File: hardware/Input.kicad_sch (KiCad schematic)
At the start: 40 parts, among them J1 USB_C_Receptacle_USB2.0, J2 Barrel_Jack_Switch, J4 AudioJack3, J5 Conn_Coaxial, J6 Conn_Coaxial, J7 Conn_Coaxial, J8 Conn_Coaxial, U23 74LVCH2T45DC, U24 74LVCH2T45DC, U25 74LVCH2T45DC

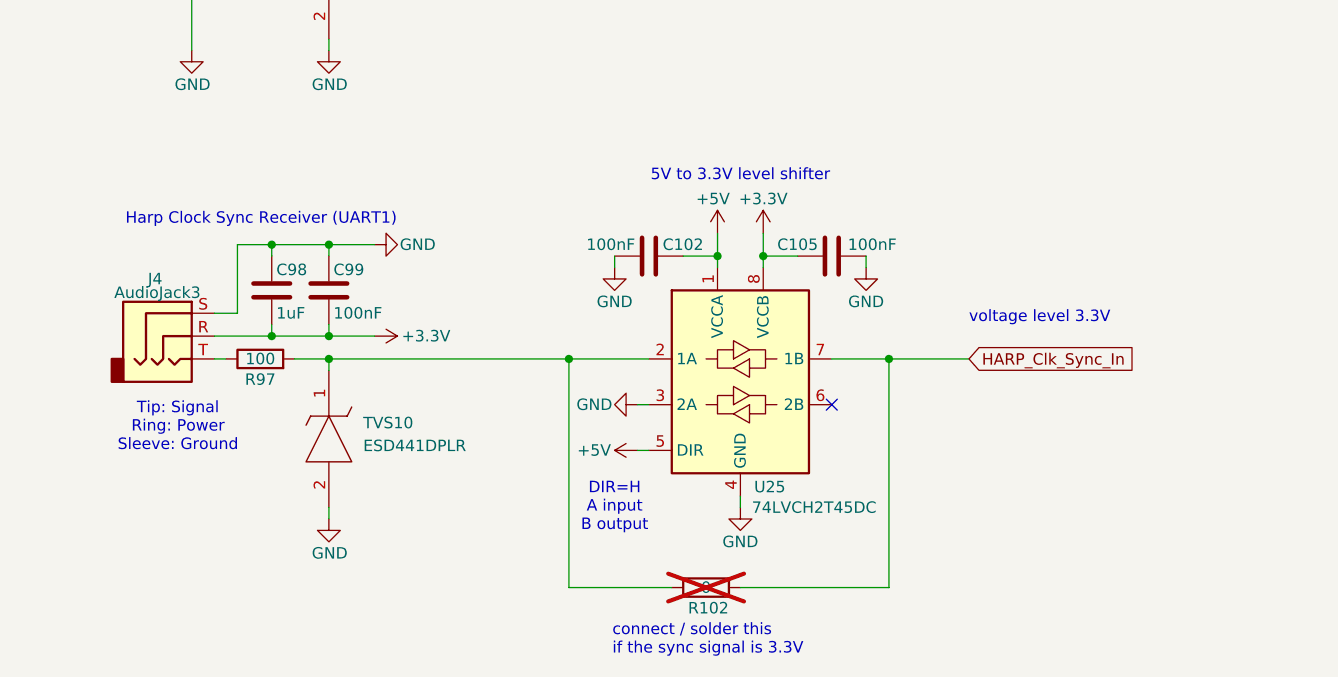
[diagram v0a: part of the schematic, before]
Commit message: draft simplified rp2350 schematic w/sd card
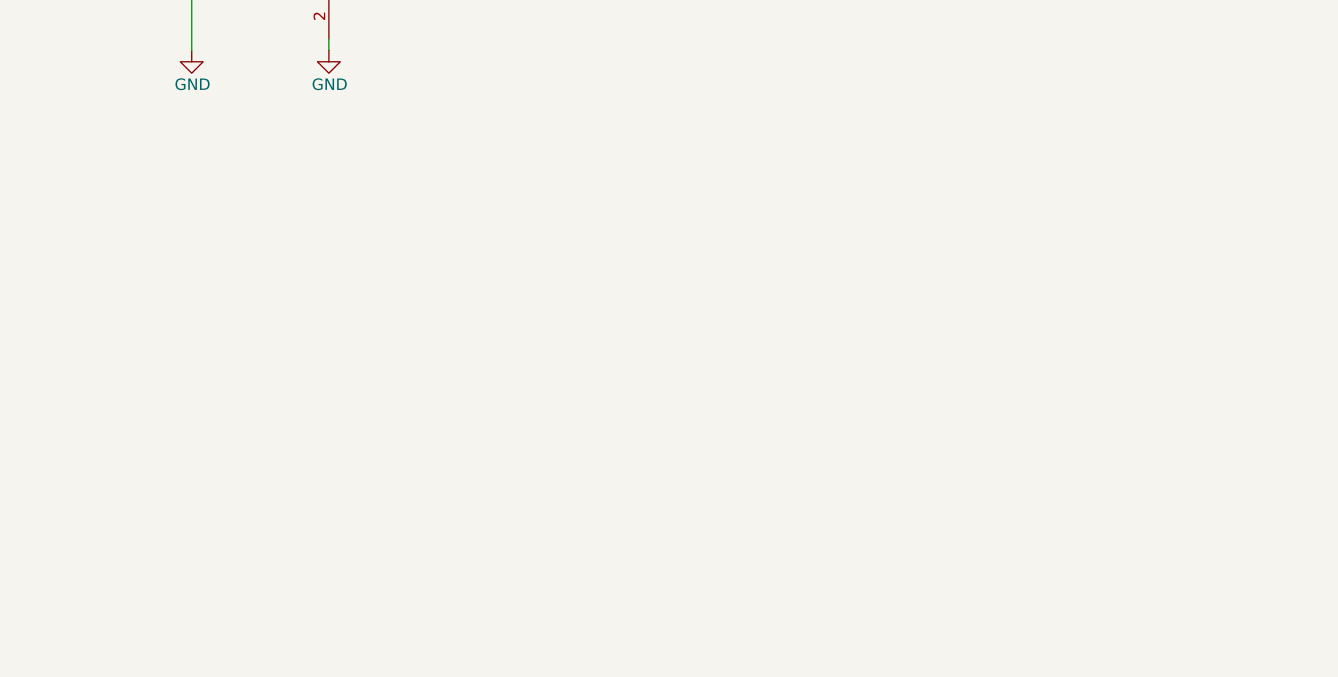
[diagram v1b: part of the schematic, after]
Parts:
- removed C102, C105, C99: 100nF, Capacitor_SMD:C_0603_1608Metric, symbol harp.device.quad.dac:C_0603
- removed C98: 1uF, Capacitor_SMD:C_0603_1608Metric, symbol harp.device.quad.dac:C_0603
- removed J4: AudioJack3, harp.device.quad.dac.kicad:Jack_3.5mm_CUI_SJ-3524-SMT_Horizontal, symbol harp.device.quad.dac:AudioJack3
- removed R102: 0, Resistor_SMD:R_0603_1608Metric, symbol harp.device.quad.dac:R_0603
- removed R97: 100, Resistor_SMD:R_0603_1608Metric, symbol harp.device.quad.dac:R_0603
- removed TVS10: ESD441DPLR, harp.device.quad.dac.kicad:ESD441DPLR, symbol harp.device.quad.dac:ESD441DPLR
- removed U25: 74LVCH2T45DC, harp.device.quad.dac.kicad:VSSOP-8_2.3x2mm_P0.5mm, symbol harp.device.quad.dac:74LVCH2T45DC
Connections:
- no-connect marks 8 -> 7
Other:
- note removed: "Harp Clock Sync Receiver (UART1)"
- note removed: "Tip: Signal Ring: Power Sleeve: Ground"
- note removed: "connect / solder this if the sync signal is 3.3V"

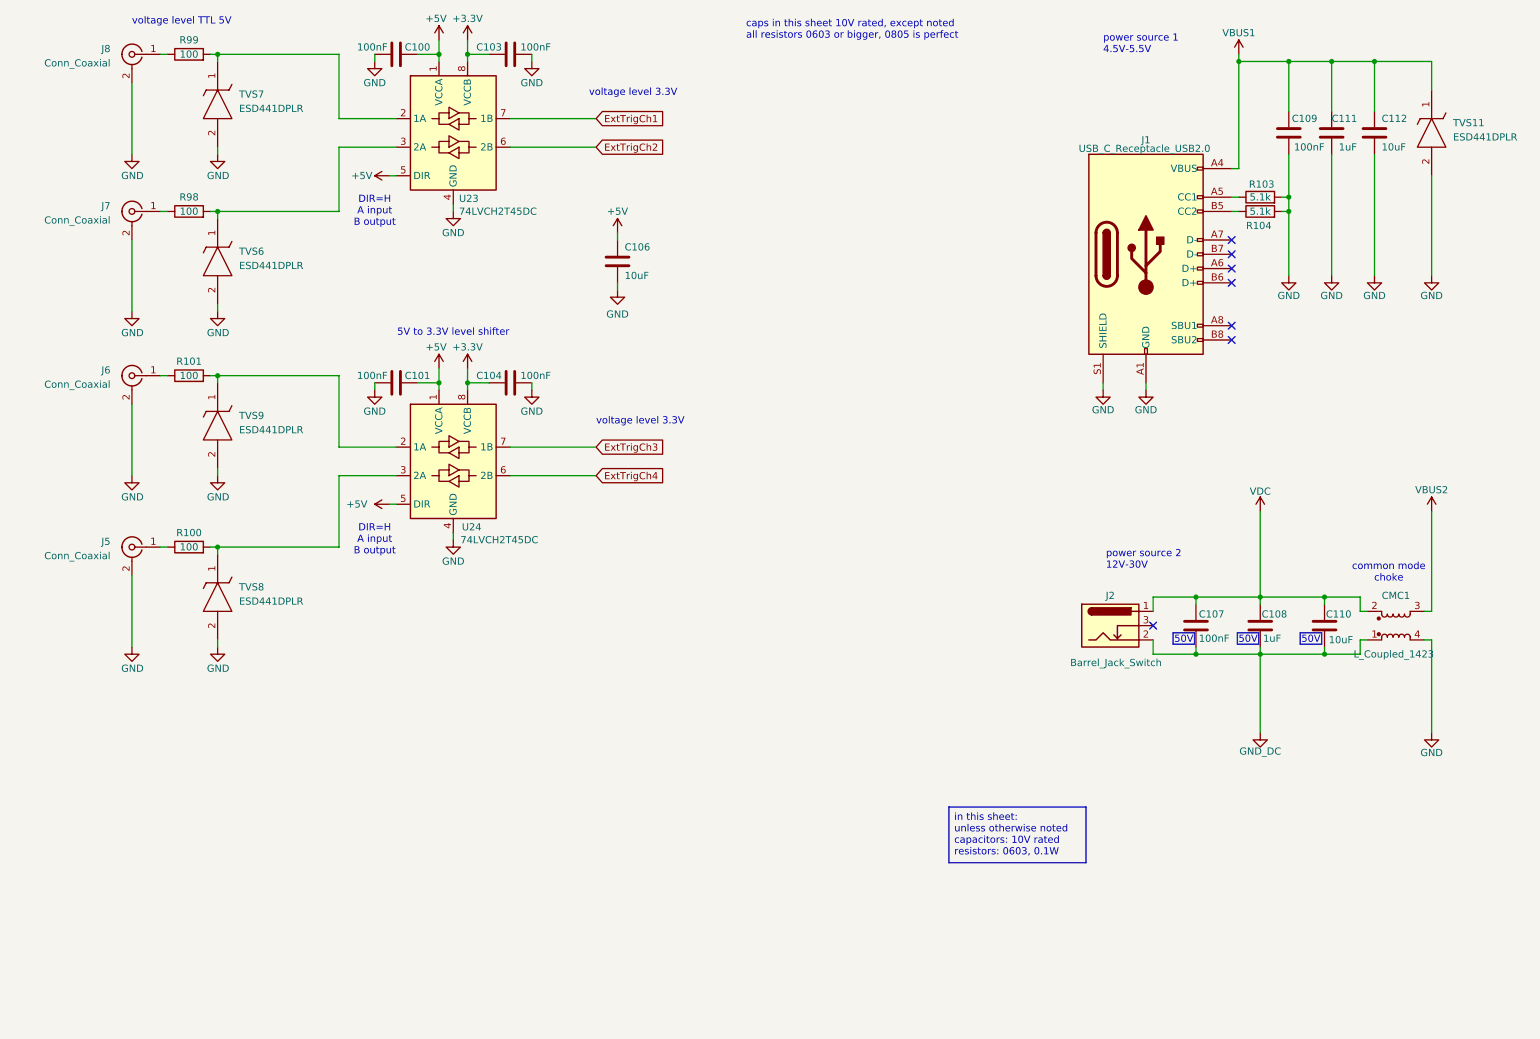
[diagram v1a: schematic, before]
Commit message: draft new analog signal chain & short-circuit detection
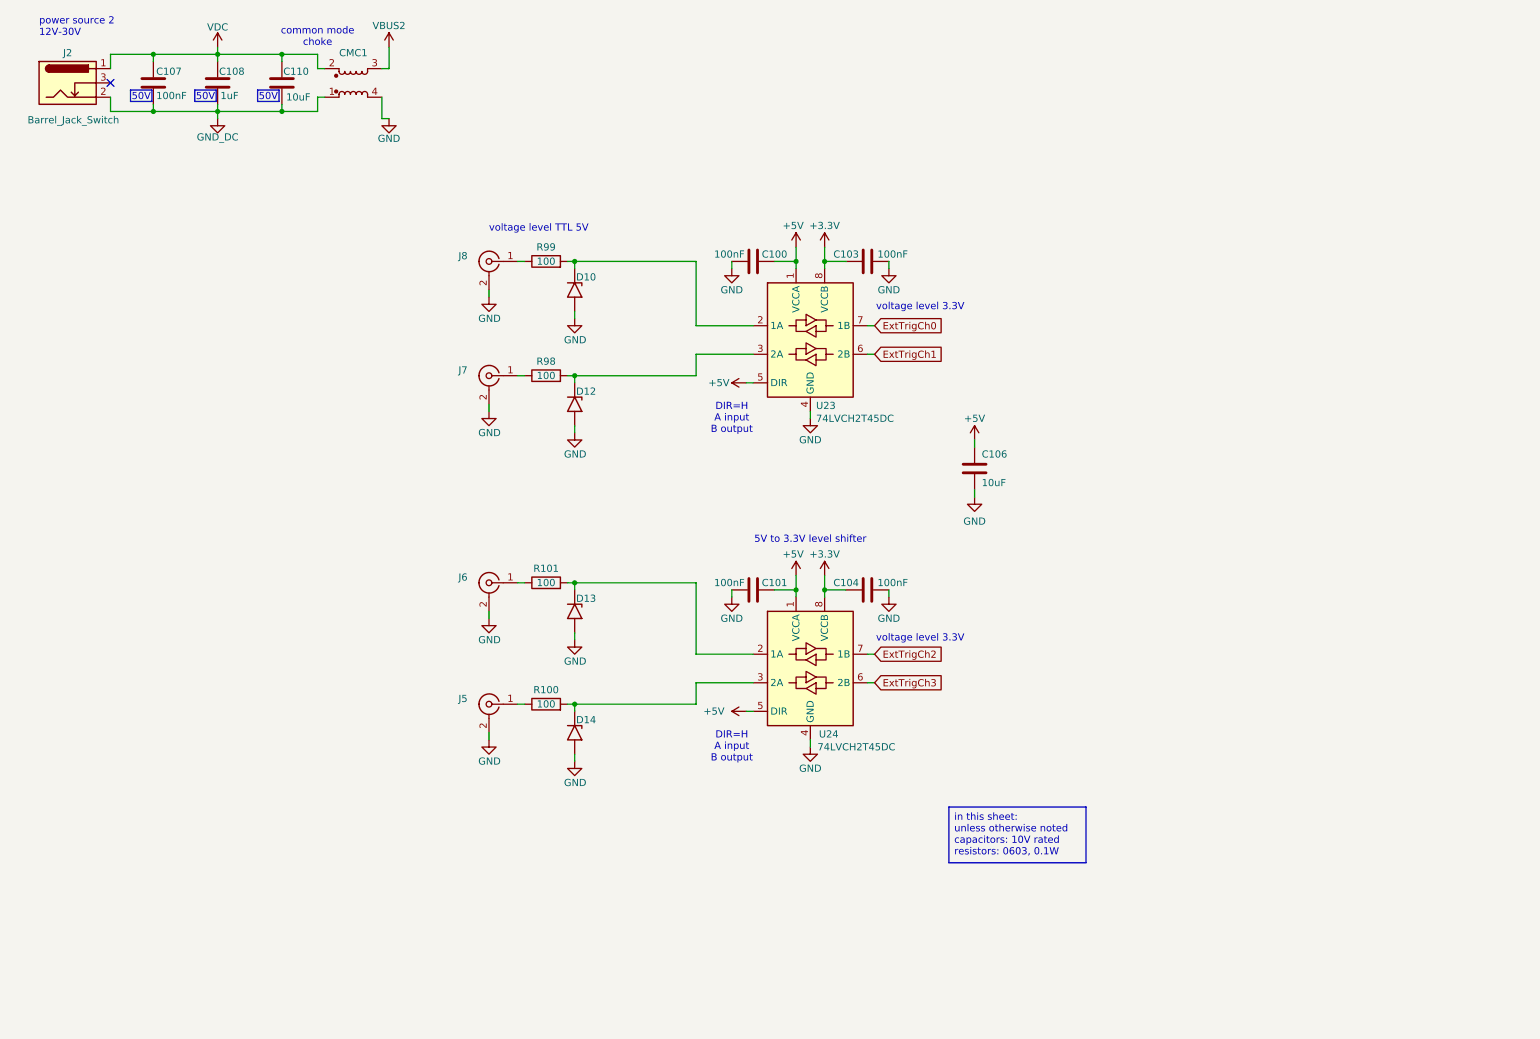
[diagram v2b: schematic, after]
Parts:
- removed C109: 100nF, Capacitor_SMD:C_0603_1608Metric, symbol harp.device.quad.dac:C_0603
- removed C111: 1uF, Capacitor_SMD:C_0603_1608Metric, symbol harp.device.quad.dac:C_0603
- removed C112: 10uF, Capacitor_SMD:C_0603_1608Metric, symbol harp.device.quad.dac:C_0603
- removed J1: USB_C_Receptacle_USB2.0, harp.device.quad.dac.kicad:USB_C_Receptacle_JAE_DX07S016JA1R1500, symbol harp.device.quad.dac:USB_C_Receptacle_USB2.0
- removed R103, R104: 5.1k, Resistor_SMD:R_0603_1608Metric, symbol harp.device.quad.dac:R_0603
- removed TVS11, TVS6, TVS7, TVS8, TVS9: ESD441DPLR, harp.device.quad.dac.kicad:ESD441DPLR, symbol harp.device.quad.dac:ESD441DPLR
- added D10, D12, D13, D14: VBUS05N1-HD1-G3-08, Diode_SMD:D_SOD-882, symbol kicad_component_library:VBUS05N1-HD1-G3-08
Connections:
- net ExtTrigCh4 is gone; now on net ExtTrigCh3: U24.6 (2B)
- net ExtTrigCh1: now also U23.6 (2B); no longer U23.7 (1B)
- net ExtTrigCh2: now also U24.7 (1B); no longer U23.6 (2B)
- net ExtTrigCh3: no longer U24.7 (1B)
- net GND: now also D10.2 (A2), D12.2 (A2), D13.2 (A2), D14.2 (A2)
- net at R99.2, U23.2 (1A): now also D10.1 (A1)
- net at R98.2, U23.3 (2A): now also D12.1 (A1)
- net at R100.2, U24.3 (2A): now also D14.1 (A1)
- net at R101.2, U24.2 (1A): now also D13.1 (A1)
- new net ExtTrigCh0: U23.7 (1B)
- no-connect marks 7 -> 1
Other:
- note removed: "caps in this sheet 10V rated, except noted all resistors 0603 or bigger, 0805 is perfect"
- note removed: "power source 1 4.5V-5.5V"
- moved on the sheet: C100, C101, C103, C104, C106, C107, C108, C110, CMC1, J2, J5, J6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

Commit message: draft split rail power supply design
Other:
- note added: "??V-30V"
- note removed: "power source 2 12V-30V"
- moved on the sheet: C108, C110, CMC1, D10, D12, D13, D14, J5, J6, J7, J8, R100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

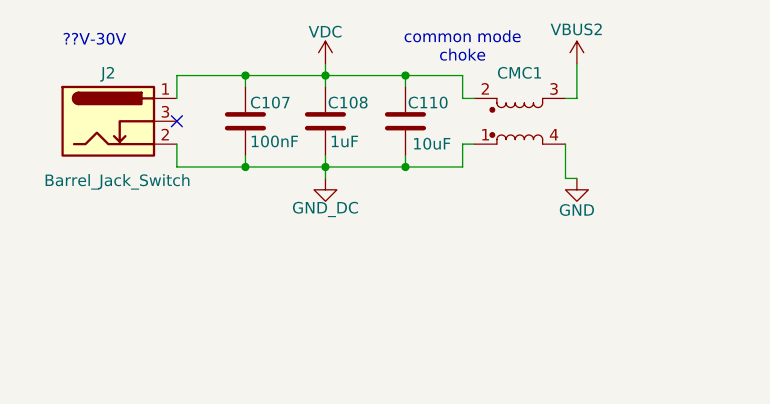
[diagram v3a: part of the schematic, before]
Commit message: cleanup power supply chain
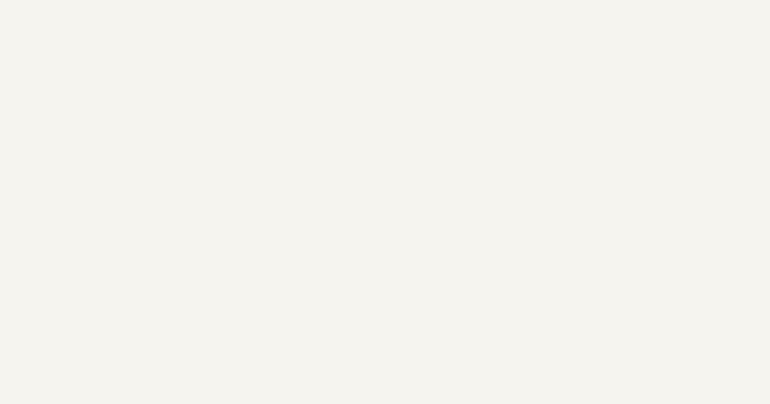
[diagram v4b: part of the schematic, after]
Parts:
- removed C107: 100nF, Capacitor_SMD:C_0603_1608Metric, symbol harp.device.quad.dac:C_0603
- removed C108: 1uF, Capacitor_SMD:C_0603_1608Metric, symbol harp.device.quad.dac:C_0603
- removed C110: 10uF, Capacitor_SMD:C_0603_1608Metric, symbol harp.device.quad.dac:C_0603
- removed CMC1: L_Coupled_1423, harp.device.quad.dac.kicad:L_CommonModeChoke_TDKCorporation_1210, symbol harp.device.quad.dac:L_Coupled_1423
- removed J2: Barrel_Jack_Switch, harp.device.quad.dac.kicad:BarrelJack_CUI_PJ-102AH_Horizontal, symbol harp.device.quad.dac:Barrel_Jack_Switch
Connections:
- no-connect marks 1 -> 0
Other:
- note removed: "??V-30V"
- note removed: "common mode choke"

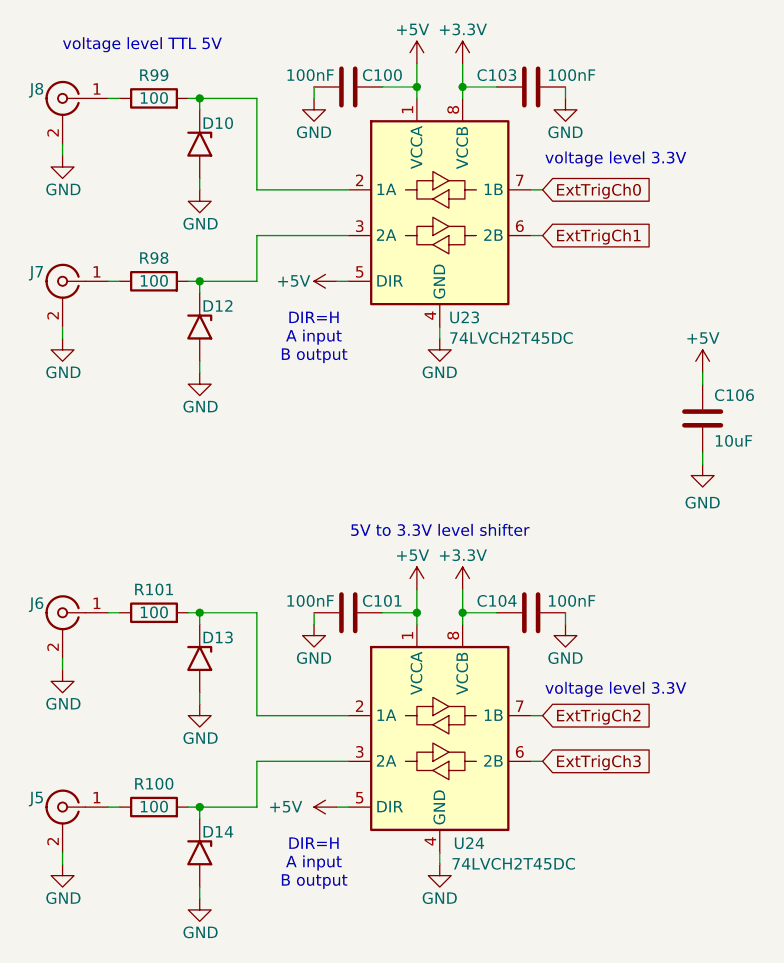
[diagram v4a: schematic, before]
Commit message: update tvs diodes, regulators, and power supply chain
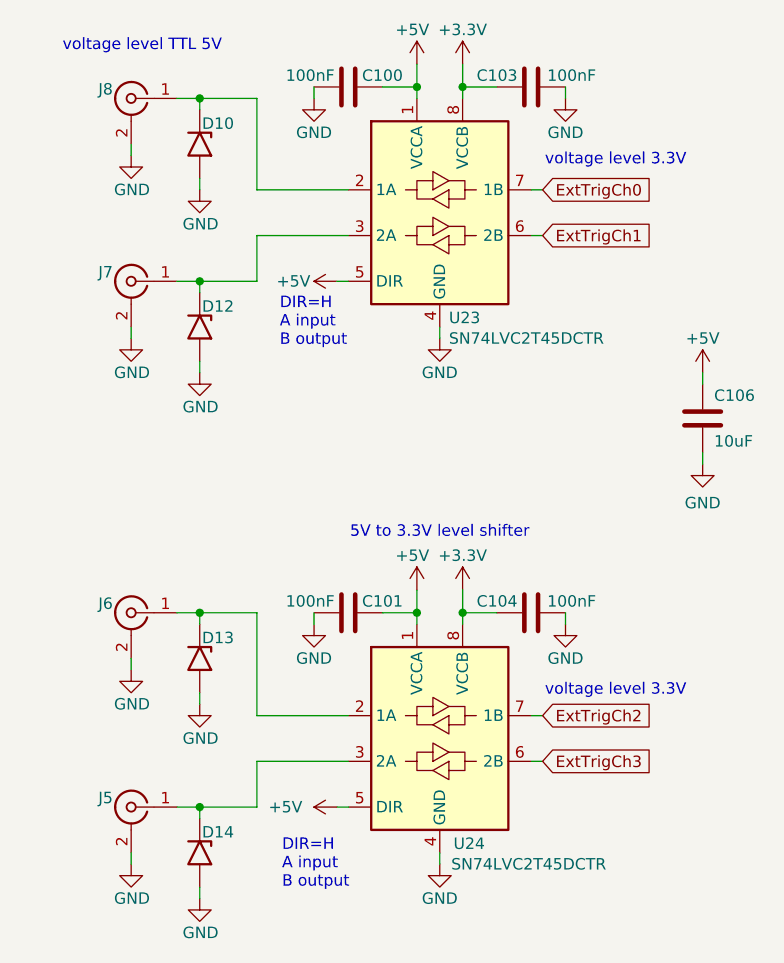
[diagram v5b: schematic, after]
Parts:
- removed R100, R101, R98, R99: 100, Resistor_SMD:R_0603_1608Metric, symbol harp.device.quad.dac:R_0603
- C100, C101, C103, C104: Manufacturer Number (none) -> C0603C104K5RACTU
- C106: Manufacturer Number (none) -> GRM188R61E106KA73D
- J5, J6, J7, J8: Manufacturer Number (none) -> CONSMA002-SMD-G-T; Manufacturer_Name TE Connectivity Linx -> (none); Manufacturer_Part_Number CONSMA002-SMD-G-T -> (none)
- U23, U24: value 74LVCH2T45DC -> SN74LVC2T45DCTR; Link https://www.digikey.com/en/products/detail/nexperia-usa-inc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 -> https://www.digikey.com/en/products/detail/texas-instrument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; Manufacturer Nexperia -> Texas Instruments; Manufacturer Number 74LVCH2T45DC,125 -> SN74LVC2T45DCTR; Manufacturer_Name Nexperia -> (none); Manufacturer_Part_Number 74LVCH2T45DC,125 -> (none)
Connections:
- net at D14.1 (A1), U24.3 (2A): now also J5.1 (In)
- net at D10.1 (A1), U23.2 (1A): now also J8.1 (In)
- net at D12.1 (A1), U23.3 (2A): now also J7.1 (In)
- net at J6.1 (In): now also D13.1 (A1), U24.2 (1A)
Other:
- moved on the sheet: J5, J6, J7, J8

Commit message: update short detection; draft bom
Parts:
- C100, C101, C103, C104: footprint Capacitor_SMD:C_0603_1608Metric -> Capacitor_SMD:C_0402_1005Metric; Link https://www.digikey.com/en/products/detail/kemet/C0603C104K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 -> https://www.digikey.com/en/products/detail/murata-electroni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; Manufacturer KEMET -> Murata Electronics; Manufacturer Number C0603C104K5RACTU -> GRM155R71H104KE14D; Manufacturer_Name KEMET -> (none); Manufacturer_Part_Number C0603C104K5RACTU -> (none); PCBWay Link https://www.pcbway.com/components/detail/0402B104K160CT/307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 -> (none); Temperature Coefficient (none) -> X7R
- C106: Alternate CL21B106KOQNNNE -> (none); Manufacturer_Name Murata Electronics -> (none); Manufacturer_Part_Number GRM188R61E106KA73D -> (none); Temperature Coefficient (none) -> X5R
- D10, D12, D13, D14: Link (none) -> https://www.digikey.com/en/products/detail/vishay-general-s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; Manufacturer (none) -> Vishay General Semiconductor - Diodes Division; Manufacturer Number (none) -> VBUS05N1-HD1-G3-08

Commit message: update board draft
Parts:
- J10: renamed from J8; footprint harp.device.quad.dac.kicad:SMA_TE_Connectivity_CONSMA002-SMD-G-T_Horizontal -> kicad-lib:BNC_TEConnectivity_CONBNC001_Vertical; Link https://www.digikey.com/en/products/detail/te-connectivity-linx/CONSMA002-SMD-G-T/10524518 -> https://www.digikey.com/en/products/detail/te-connectivity-linx/CONBNC001/16013844; Manufacturer Number CONSMA002-SMD-G-T -> CONBNC001
- J11: renamed from J7; footprint harp.device.quad.dac.kicad:SMA_TE_Connectivity_CONSMA002-SMD-G-T_Horizontal -> kicad-lib:BNC_TEConnectivity_CONBNC001_Vertical; Link https://www.digikey.com/en/products/detail/te-connectivity-linx/CONSMA002-SMD-G-T/10524518 -> https://www.digikey.com/en/products/detail/te-connectivity-linx/CONBNC001/16013844; Manufacturer Number CONSMA002-SMD-G-T -> CONBNC001
- J12: renamed from J6; footprint harp.device.quad.dac.kicad:SMA_TE_Connectivity_CONSMA002-SMD-G-T_Horizontal -> kicad-lib:BNC_TEConnectivity_CONBNC001_Vertical; Link https://www.digikey.com/en/products/detail/te-connectivity-linx/CONSMA002-SMD-G-T/10524518 -> https://www.digikey.com/en/products/detail/te-connectivity-linx/CONBNC001/16013844; Manufacturer Number CONSMA002-SMD-G-T -> CONBNC001
- J13: renamed from J5; footprint harp.device.quad.dac.kicad:SMA_TE_Connectivity_CONSMA002-SMD-G-T_Horizontal -> kicad-lib:BNC_TEConnectivity_CONBNC001_Vertical; Link https://www.digikey.com/en/products/detail/te-connectivity-linx/CONSMA002-SMD-G-T/10524518 -> https://www.digikey.com/en/products/detail/te-connectivity-linx/CONBNC001/16013844; Manufacturer Number CONSMA002-SMD-G-T -> CONBNC001
- U22: renamed from U23; footprint harp.device.quad.dac.kicad:VSSOP-8_2.3x2mm_P0.5mm -> Package_SO:VSSOP-8_2.3x2mm_P0.5mm
- U23: renamed from U24; footprint harp.device.quad.dac.kicad:VSSOP-8_2.3x2mm_P0.5mm -> Package_SO:VSSOP-8_2.3x2mm_P0.5mm
- renumbered C100 to C59, C101 to C60, C103 to C61, C104 to C62, C106 to C63, D10 to D11
